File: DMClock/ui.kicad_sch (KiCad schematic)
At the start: 142 parts, among them U3 HV5622PG-G, U4 HV5622PG-G, U5 HV5622PG-G

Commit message: finished v.1
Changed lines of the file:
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@@
   )
   (symbol (lib_id "Connector:TestPoint") (at 223.6366 20.955 0) (unit 1)
-    (in_bom yes) (on_board yes) (dnp no) (fields_autoplaced)
-    (property "Reference" "TP31" (at 225.1606 16.383 0)
+    (in_bom yes) (on_board yes) (dnp no)
+    (property "Reference" "TP31" (at 225.1606 16.383 90)
       (effects (font (size 1.27 1.27)) (justify left))
     )
@@
     )
   )
-  (symbol (lib_id "power:GND") (at 228.6 18.161 180) (unit 1)
-    (in_bom yes) (on_board yes) (dnp no)
-    (property "Reference" "#PWR025" (at 228.6 11.811 0)
-      (effects (font (size 1.27 1.27)) hide)
-    )
-    (property "Value" "GND" (at 230.759 16.891 0)
-      (effects (font (size 1.27 1.27)) (justify right))
-    )
-    (property "Footprint" "" (at 228.6 18.161 0)
-      (effects (font (size 1.27 1.27)) hide)
-    )
-    (property "Datasheet" "" (at 228.6 18.161 0)
-      (effects (font (size 1.27 1.27)) hide)
-    )
-    (pin "1")
-    (instances
-      (project "DMClock"
-        (path "/b42b345f-a3f2-4eff-9109-2f4619119d33/6e102def-f8db-44ea-948b-b7115f90d225"
-          (reference "#PWR025") (unit 1)
-        )
-      )
-    )
-  )
   (symbol (lib_id "Connector:TestPoint") (at 142.1952 73.787 180) (unit 1)
     (in_bom yes) (on_board yes) (dnp no) (fields_autoplaced)
@@
   )
   (symbol (lib_id "Connector:TestPoint") (at 226.1225 20.955 0) (unit 1)
-    (in_bom yes) (on_board yes) (dnp no) (fields_autoplaced)
-    (property "Reference" "TP32" (at 227.6465 16.383 0)
-      (effects (font (size 1.27 1.27)) (justify left))
-    )
+    (in_bom yes) (on_board yes) (dnp no)
+    (property "Reference" "TP32" (at 227.6465 16.383 90)
+      (effects (font (size 1.27 1.27)) (justify left))
+    )

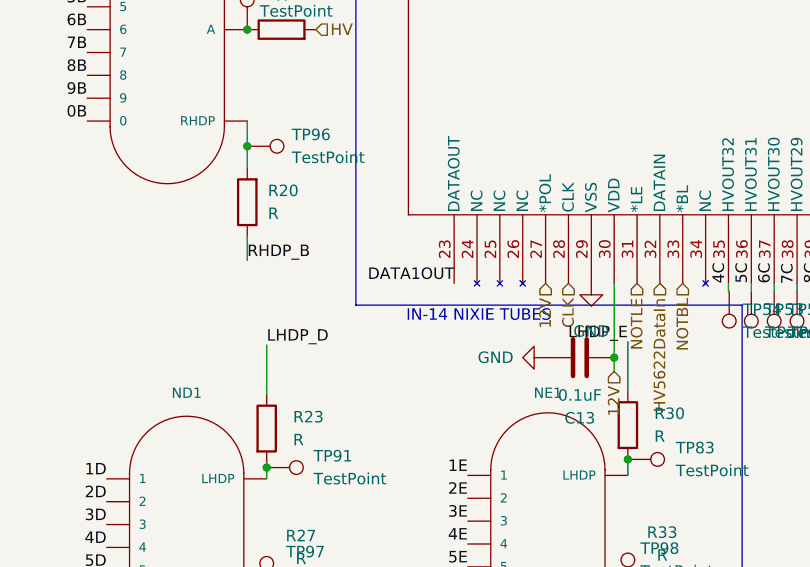
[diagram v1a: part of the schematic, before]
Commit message: updated buck converter
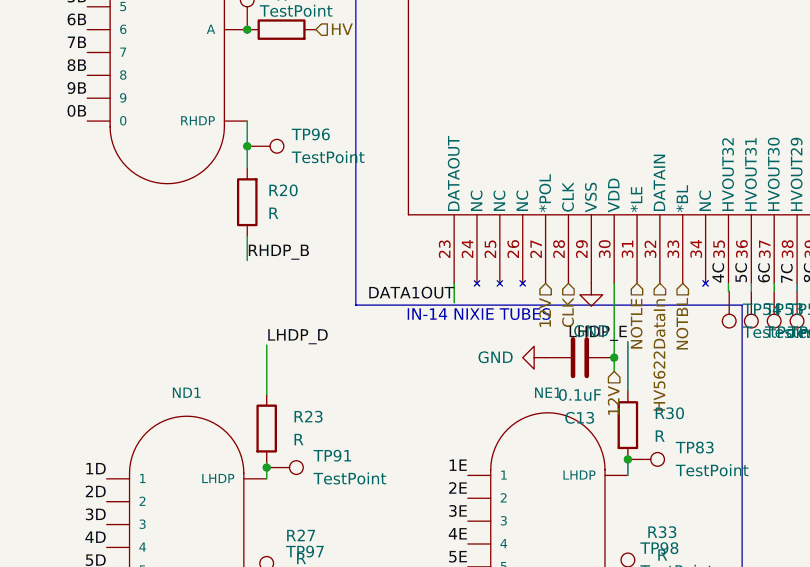
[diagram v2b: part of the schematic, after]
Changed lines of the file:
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@@
+    (stroke (width 0) (type default))
+  )
+  (wire (pts (xy 111.633 75.057) (xy 111.633 72.898))
     (stroke (width 0) (type default))
   )
@@
     (effects (font (size 1.27 1.27)) (justify right bottom))
   )
-  (label "DATA1OUT" (at 111.633 72.898 180) (fields_autoplaced)
-    (effects (font (size 1.27 1.27)) (justify right bottom))
-  )
+  (label "DATA1OUT" (at 111.633 75.057 180) (fields_autoplaced)
+    (effects (font (size 1.27 1.27)) (justify right bottom))
+  )
